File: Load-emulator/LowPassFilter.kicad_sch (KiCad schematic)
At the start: 4 parts

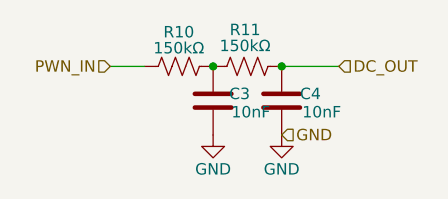
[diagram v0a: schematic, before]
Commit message: Replacement of the microcontroller w/ picoblade
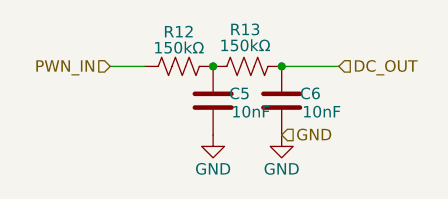
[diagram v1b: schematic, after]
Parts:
- renumbered C3 to C5, C4 to C6, R10 to R12, R11 to R13
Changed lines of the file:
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@@
 		(on_board yes)
 		(dnp no)
-		(property "Reference" "C3"
+		(property "Reference" "C5"
 			(at 138.938 89.408 0)
 			(effects
@@
 		(on_board yes)
 		(dnp no)
-		(property "Reference" "R10"
+		(property "Reference" "R12"
 			(at 133.35 82.55 90)
 			(effects
@@
 		(on_board yes)
 		(dnp no)
-		(property "Reference" "R11"
+		(property "Reference" "R13"
 			(at 140.716 82.296 90)
 			(effects
@@
 		(on_board yes)
 		(dnp no)
-		(property "Reference" "#PWR017"
+		(property "Reference" "#PWR019"
 			(at 137.16 100.33 0)
 			(effects
@@
 		(on_board yes)
 		(dnp no)
-		(property "Reference" "#PWR018"
+		(property "Reference" "#PWR020"
 			(at 144.78 100.33 0)
 			(effects
@@
 		(on_board yes)
 		(dnp no)
-		(property "Reference" "C4"
+		(property "Reference" "C6"
 			(at 146.812 89.408 0)
 			(effects

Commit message: Added footprints for the remaining resistors, capacitors and ampops, as well as some 3D models
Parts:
- C5, C6: footprint (none) -> Capacitor_SMD:C_0201_0603Metric
- R12, R13: footprint (none) -> Resistor_SMD:R_0201_0603Metric
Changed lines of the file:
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@@
 			)
 		)
-		(property "Footprint" ""
+		(property "Footprint" "Capacitor_SMD:C_0201_0603Metric"
 			(at 138.1252 93.98 0)
 			(effects
@@
 			)
 		)
-		(property "Footprint" ""
+		(property "Footprint" "Resistor_SMD:R_0201_0603Metric"
 			(at 133.604 85.344 90)
 			(effects
@@
 			)
 		)
-		(property "Footprint" ""
+		(property "Footprint" "Resistor_SMD:R_0201_0603Metric"
 			(at 141.224 85.344 90)
 			(effects
@@
 			)
 		)
-		(property "Footprint" ""
+		(property "Footprint" "Capacitor_SMD:C_0201_0603Metric"
 			(at 145.7452 93.98 0)
 			(effects
